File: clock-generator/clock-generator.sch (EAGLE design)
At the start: 85 parts, among them IC1 24C00TS, K2 694108106102, M1 MENTOR_12701001, U1 SN74LVC1G04DBV, U3 ATSAMD11-QFN24, U4 SI5351C, U5 IP4234CZ6, U6 IP4234CZ6, U7 VCTCXO-CONNORWINFIELD, X1 MINI-USB-SHIELD-UX60A-MB-5ST, X2 JACK2.5_SJ-2523, X4 UEXT/90

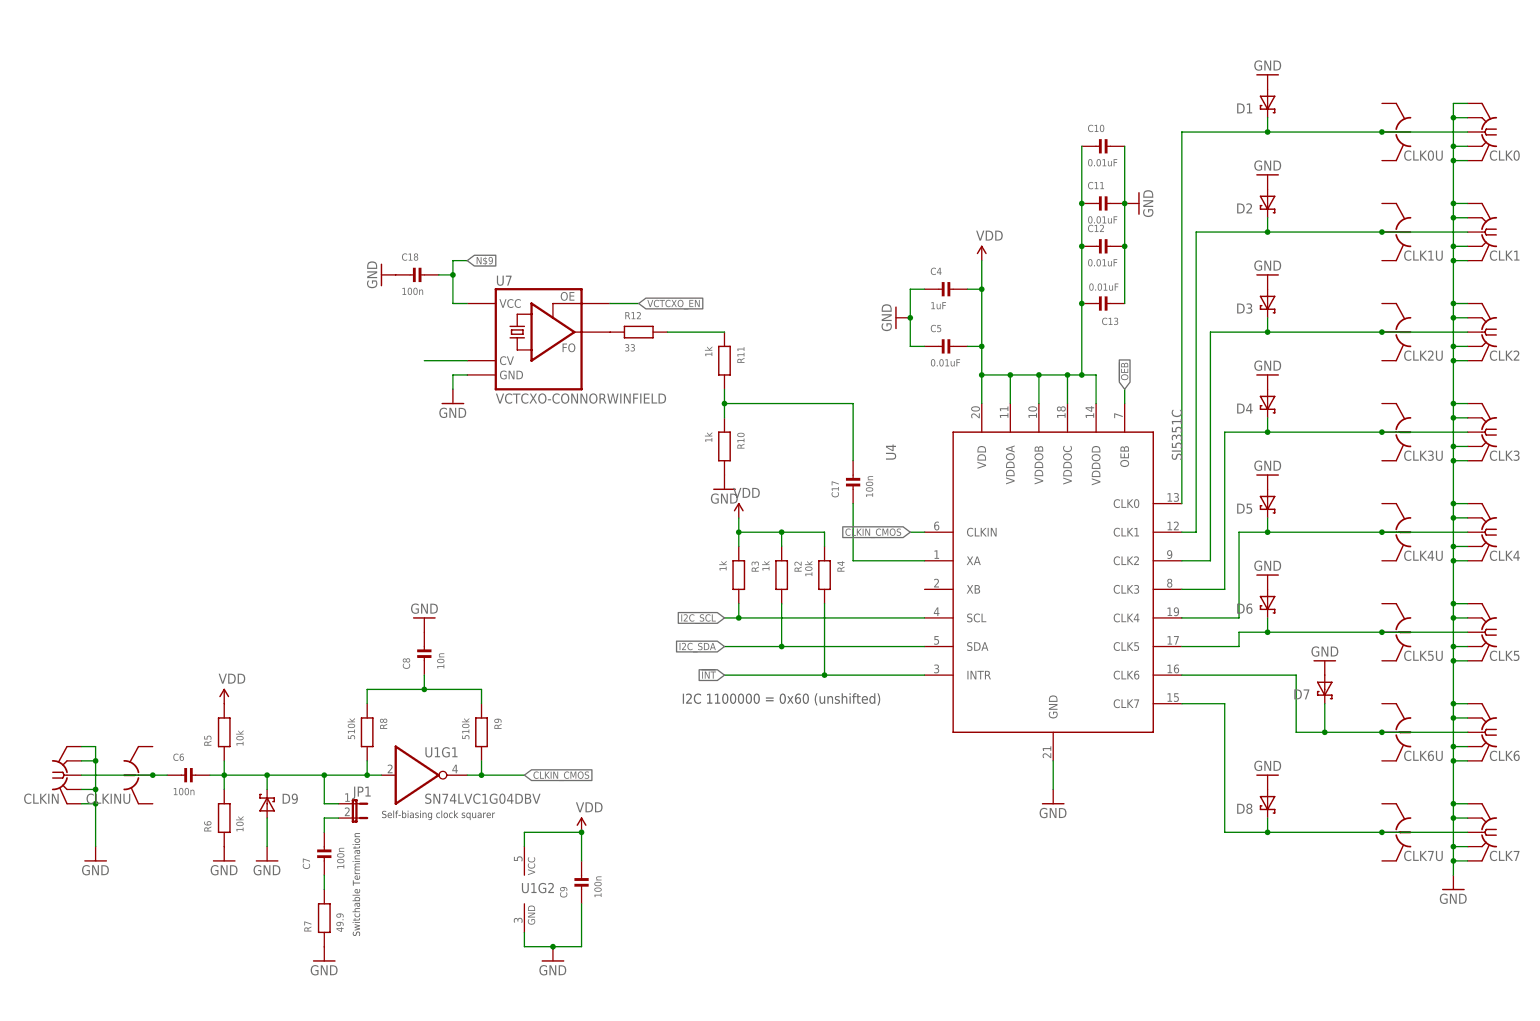
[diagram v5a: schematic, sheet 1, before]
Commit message: clock-gen: finish routing of PCB layout
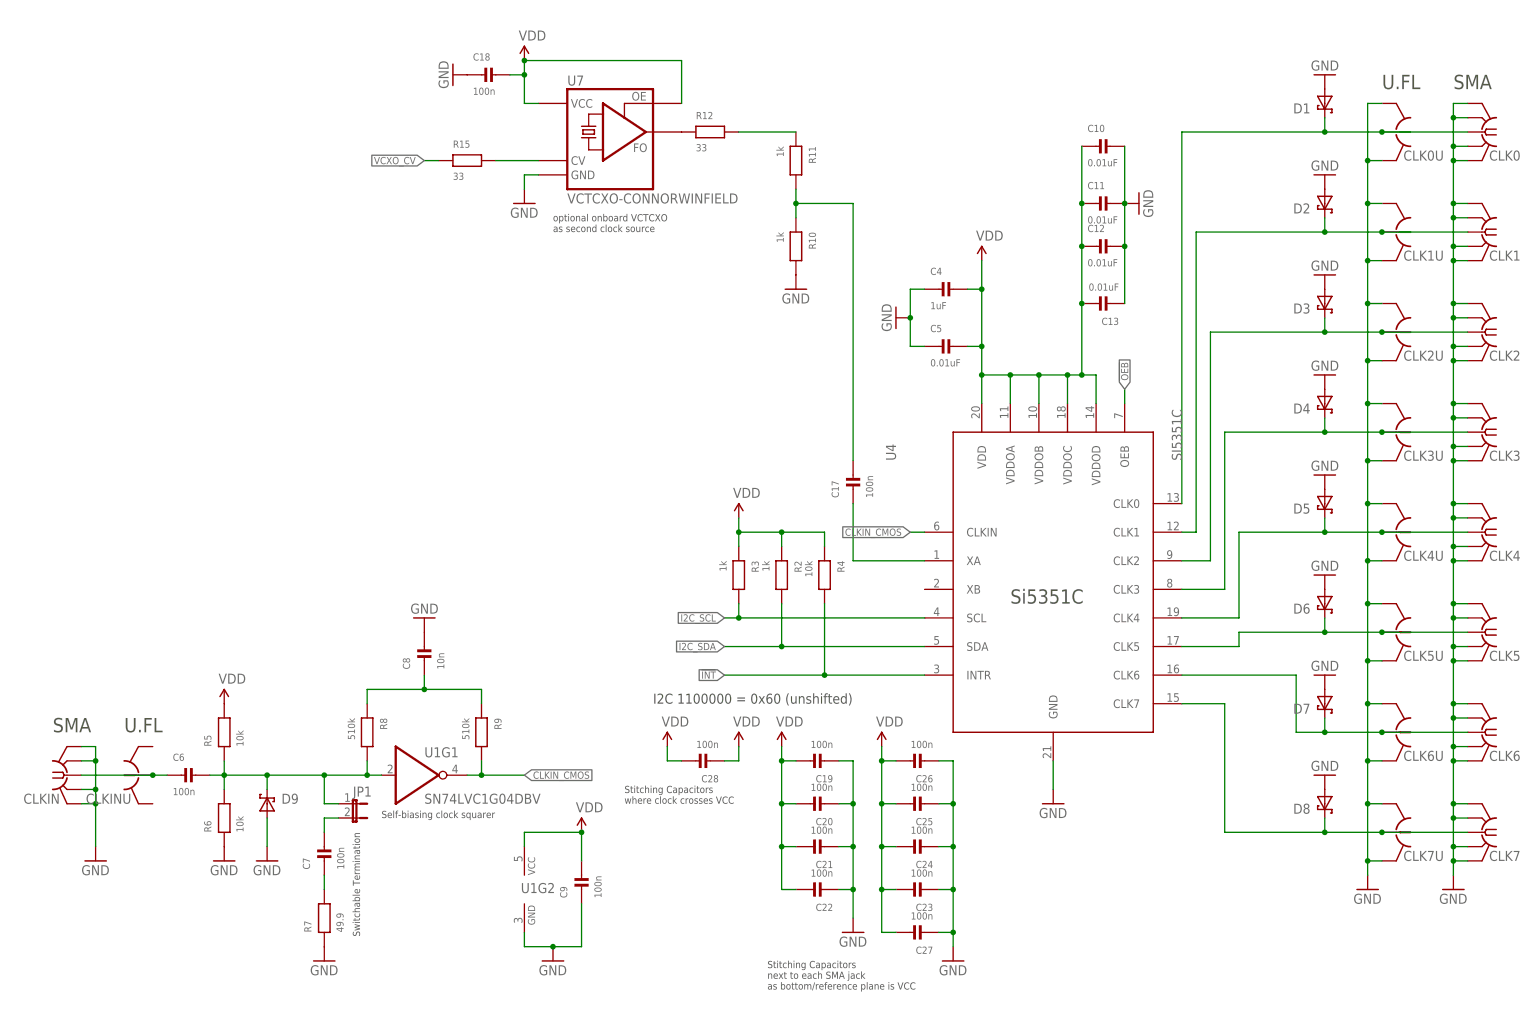
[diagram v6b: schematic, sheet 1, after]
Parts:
- added C19, C20, C21, C22, C23, C24, C25, C26, C27, C28: 100n, rc-sysmocom:CAP_CERAMIC_0603
- added D11, D12: CUS08F30, diodes-sysmocom:DIODE-SCHOTTKY-SOD-323
- added R15: 33, rc-sysmocom:RESISTOR_0603
- added R16: 30k, rc-sysmocom:RESISTOR_0603
- added R17: 47k, rc-sysmocom:RESISTOR_0603
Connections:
- removed net N$8: U6.1A, X2.MIDDLE, X3.2
- removed net N$9: C18.2, U7.VCC
- removed net VCTCXO_EN: U7.OE
- new net UART_RX0: U6.2A, X2.TIP, X3.3, X4.RXD
- new net UART_TX0: U6.1A, X2.MIDDLE, X3.2, X4.TXD
- new net VCXO_CV: R15.1, U3.PA02/AIN0/Y0/VOUT
- net !INT: now also U3.PA03/ADCVREFA/DACVREFA/AIN1/Y1; no longer U3.PA02/AIN0/Y0/VOUT
- net GND: now also C19.1, C20.1, C21.1, C22.1, C23.1, C24.1, C25.1, C26.1, C27.1, CLK0U.GND@1, CLK0U.GND@2, CLK1U.GND@1, CLK1U.GND@2, CLK2U.GND@1, CLK2U.GND@2, CLK3U.GND@1, CLK3U.GND@2, CLK4U.GND@1, CLK4U.GND@2, CLK5U.GND@1, CLK5U.GND@2, CLK6U.GND@1, CLK6U.GND@2, CLK7U.GND@1, CLK7U.GND@2, R17.1
- net N$10: now also R15.2
- net N$15: now also D11.A; no longer F1.2
- net N$6: now also D11.C, D12.C, F1.2; no longer U6.2A, X2.TIP, X3.3
- net UART_RX: no longer X4.RXD
- net UART_TX: no longer X4.TXD
- net VBUS: now also D12.A, R16.2
- net VBUS_DET: now also R16.1, R17.2
- net VDD: now also C18.2, C19.2, C20.2, C21.2, C22.2, C23.2, C24.2, C25.2, C26.2, C27.2, C28.1, C28.2, U7.OE, U7.VCC
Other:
- note added: "External 5V PSU"
- note added: "Internal 5V PSU"
- note added: "Olimex-Compatible UEXT"
- note added: "Osmocom-style 3.3V UART on 2.5mm stereo"
- note added: "Pigtail to Lumberg KLB13 panel-mount jack"
- note added: "SMA"
- note added: "Si5351C"
- note added: "Stitching Capacitors next to each SMA jack as bottom/reference plane is VCC"
- note added: "Stitching Capacitors where clock crosses VCC"
- note added: "Tag-Connect TC-2030 connector for SWD Flashing/Debugging"
- note added: "U.FL"
- note added: "optional onboard VCTCXO as second clock source"
- moved on the sheet: C18, D1, D2, D3, D4, D5, D6, D7, D8, JP2, K2, LED1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

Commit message: clock-gen: Cosmetic changes
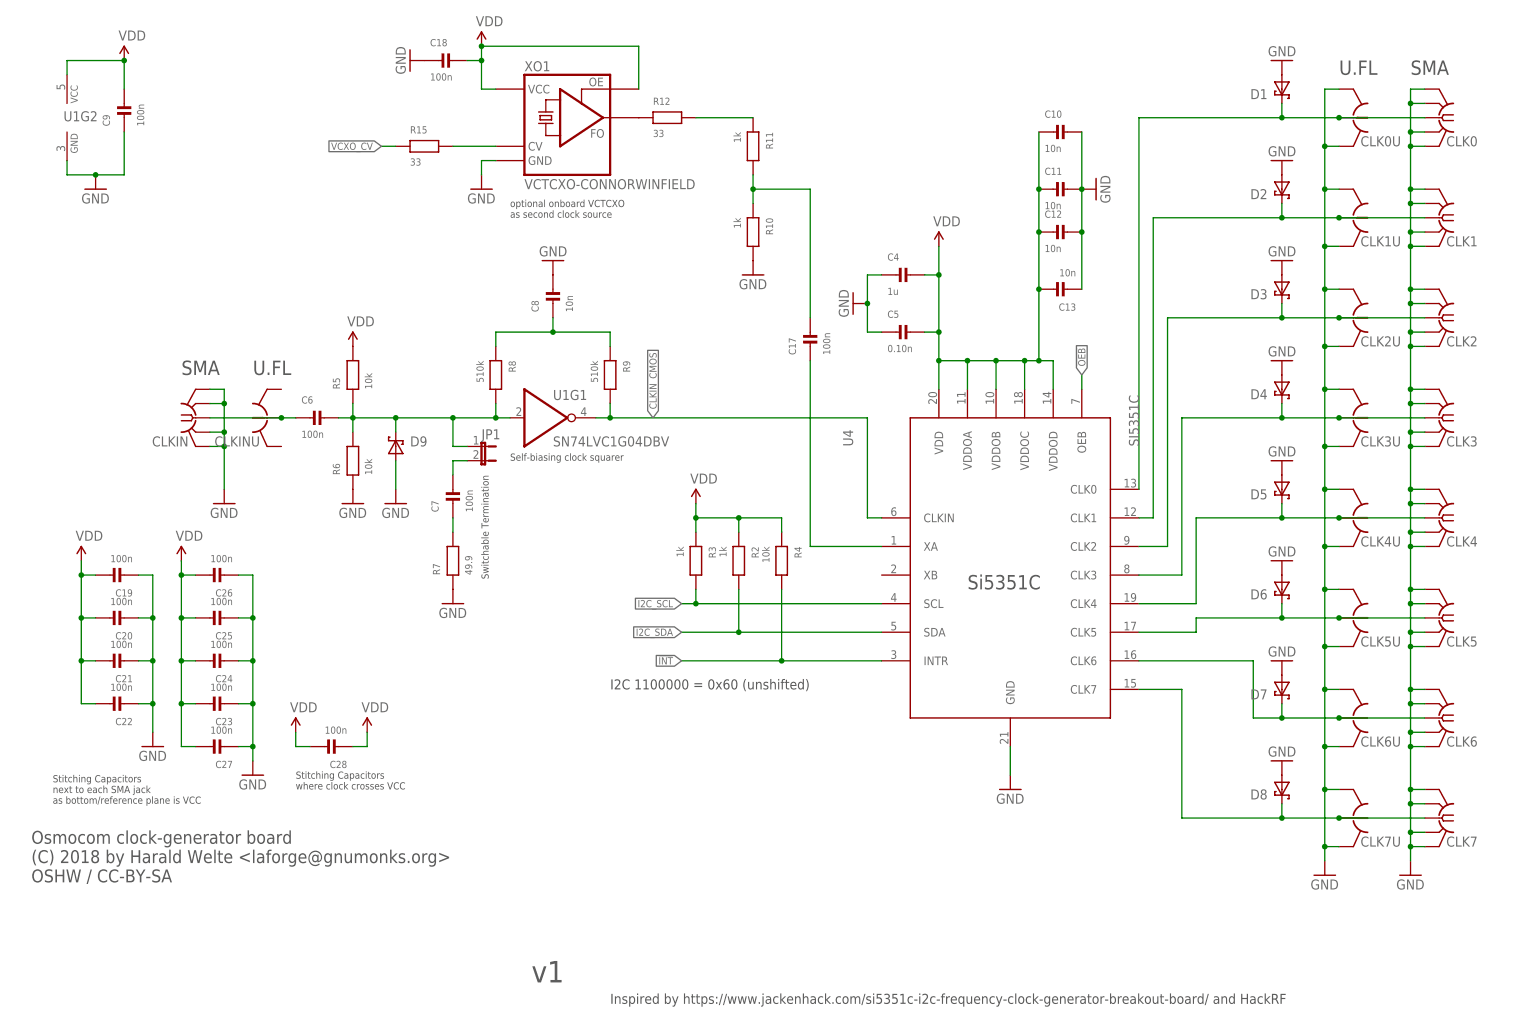
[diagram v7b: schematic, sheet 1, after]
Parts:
- removed U7: VCTCXO-CONNORWINFIELD, Connor-Winfield_VCTCXO:VCTCXO-CONNORWINFIELD
- added XO1: VCTCXO-CONNORWINFIELD, Connor-Winfield_VCTCXO:VCTCXO-CONNORWINFIELD
- C1: value 1uF -> 4.7u; device rc-sysmocom:CAP_CERAMIC_0603 -> rc-sysmocom:CAP_CERAMIC_0805
- C10, C11, C12, C13: value 0.01uF -> 10n
- C14: value (none) -> 4.7u; device rc-sysmocom:CAP_CERAMIC1206 -> rc-sysmocom:CAP_CERAMIC_0805
- C2: value 0.01uF -> 100n
- C4: value 1uF -> 1u
- C5: value 0.01uF -> 0.10n
- C701: device rc-sysmocom:CAP_CERAMIC_0603 -> rc-sysmocom:CAP_CERAMIC_0402
- C8: device rc-sysmocom:CAP_CERAMIC0603 -> rc-sysmocom:CAP_CERAMIC_0402
- U2: value (none) -> ADP151AUJZ
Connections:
- net GND: now also XO1.GND; no longer U7.GND
- net N$10: now also XO1.CV; no longer U7.CV
- net N$4: now also XO1.FO; no longer U7.FO
- net VDD: now also XO1.OE, XO1.VCC; no longer U7.OE, U7.VCC
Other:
- note added: "Connectors"
- note added: "EEPROM"
- note added: "Inspired by https://www.jackenhack.com/si5351c-i2c-frequency-clock-generator-breakout-board/ and HackRF"
- note added: "LEDs"
- note added: "Microcontroller"
- note added: "Osmocom clock-generator board (C) 2018 by Harald Welte <laforge@gnumonks.org> OSHW / CC-BY-SA"
- note added: "Power Supply"
- note added: "USB"
- moved on the sheet: C1, C10, C11, C12, C13, C14, C15, C16, C17, C18, C19, C2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

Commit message: clock-gen: Minor changes; final version as ordered
* move DC jack to extend beyond PCB edge into front panel
* harmonize component variants (10n only 0402, 4.7u only 0805)
* add "sysmocom" as manufacturer name (WEEE requirement)
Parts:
- C4: device rc-sysmocom:CAP_CERAMIC_0402 -> rc-sysmocom:CAP_CERAMIC_0603
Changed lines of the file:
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@@
 <part name="SUPPLY3" library="SparkFun-Aesthetics" deviceset="VDD" device=""/>
 <part name="C5" library="rc-sysmocom" deviceset="CAP_CERAMIC" device="_0402" value="0.10n"/>
-<part name="C4" library="rc-sysmocom" deviceset="CAP_CERAMIC" device="_0402" value="1u"/>
+<part name="C4" library="rc-sysmocom" deviceset="CAP_CERAMIC" device="_0603" value="1u"/>
 <part name="GND14" library="SparkFun-Aesthetics" deviceset="GND" device=""/>
 <part name="GND15" library="SparkFun-Aesthetics" deviceset="GND" device=""/>
